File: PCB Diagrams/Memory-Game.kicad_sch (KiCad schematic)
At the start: 32 parts, among them J1 01x02, SW1 SW_Push, SW2 SW_ON_OFF, SW3 SW_Push, SW4 SW_Push, SW5 SW_Push, SW6 SW_Push, SW7 SW_SOUND, U1 Arduino_Nano_v3

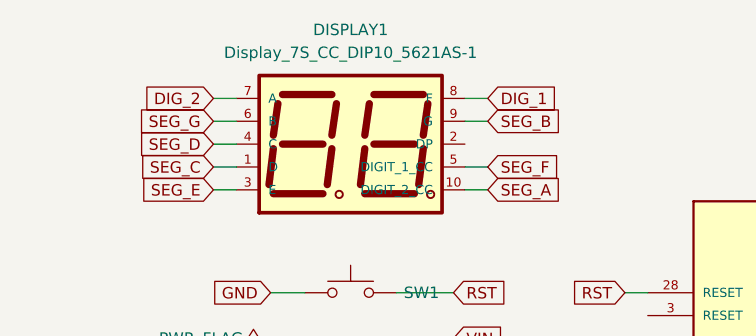
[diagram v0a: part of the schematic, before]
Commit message: Adding KiCAD 9 schematics and PCB diagrams
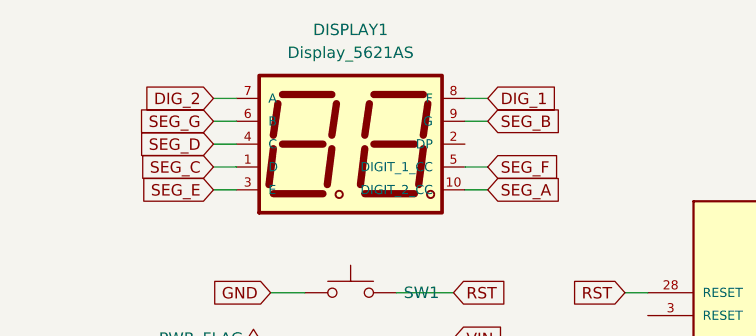
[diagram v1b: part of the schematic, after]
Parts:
- DISPLAY1: value Display_7S_CC_DIP10_5621AS-1 -> Display_5621AS
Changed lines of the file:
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@@
 			)
 		)
-		(property "Value" "Display_7S_CC_DIP10_5621AS-1"
+		(property "Value" "Display_5621AS"
 			(at 104.14 55.88 0)
 			(effects
